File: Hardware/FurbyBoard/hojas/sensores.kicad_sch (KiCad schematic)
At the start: 37 parts, among them J7 Frente: IR (emisor ×2, recept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, J8 Inclinación ×3, lengua ×2, al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, J9 Encoder ×3, leva ×2, barriga 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, Q3 AO3400A, U10 TCA9535PWR, U11 SN74LVC1G17DBVR

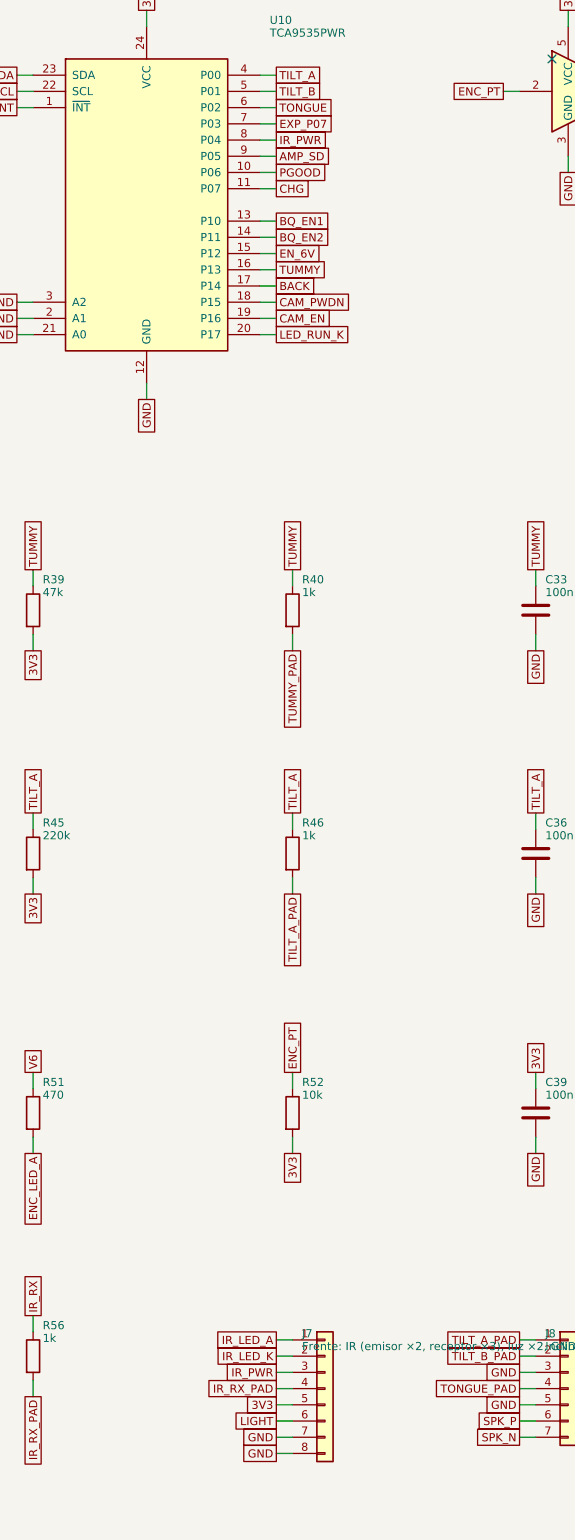
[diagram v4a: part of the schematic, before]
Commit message: Feature: IR_PWR rutado de U10 a J7 (bloque U2, 0 sin unir)
- Puertos del TCA9535 en ciclo: P03 LED_RUN_K, P04 EXP_P07, P17 IR_PWR;
  J7.3 <-> J7.8 (IR_PWR a J7.8 «RXV», J7.3 a GND). Rótulos de J7 y J_EXP.5.
- IR_PWR: vía que era de LED_RUN_K, columna de In3 x -91,4 entre LED_RUN_K
  y TUMMY, bolsa de In3 hasta una vía bajo J7.8 y In2 recto al pad.
- I2C_SCL: ramal de J11 desde la vía de U10.22 por In2 bajo U10; ramal de
  J6 a una vía nueva y B.Cu a la fila de y -69; R37.1 con 0,3.
- TONGUE recto a C35.1 y R43 0,13 mm al sur para la vía de EXP_P07.

Puerta D: ERC 0; DRC con paridad 0 violaciones, 0 sin unir, 0 paridad
(también con relleno sobre una copia); revisar-rutado PASS, 0 errores y
152 avisos (153 antes). PNG revisados: U10 (F, In3) y franja U10-J7
(F, In2, In3, B). Rellenos: GND In1/In4 1 trozo; VSYS In2 2584,5 mm² en 3
(se pierde la bolsa sin cargas bajo J7); GND F 21 y GND B 11 trozos, los
nuevos colgados del pad de J7.3.

Co-Authored-By: Claude Opus 5.5 (1M context) <noreply@anthropic.com>
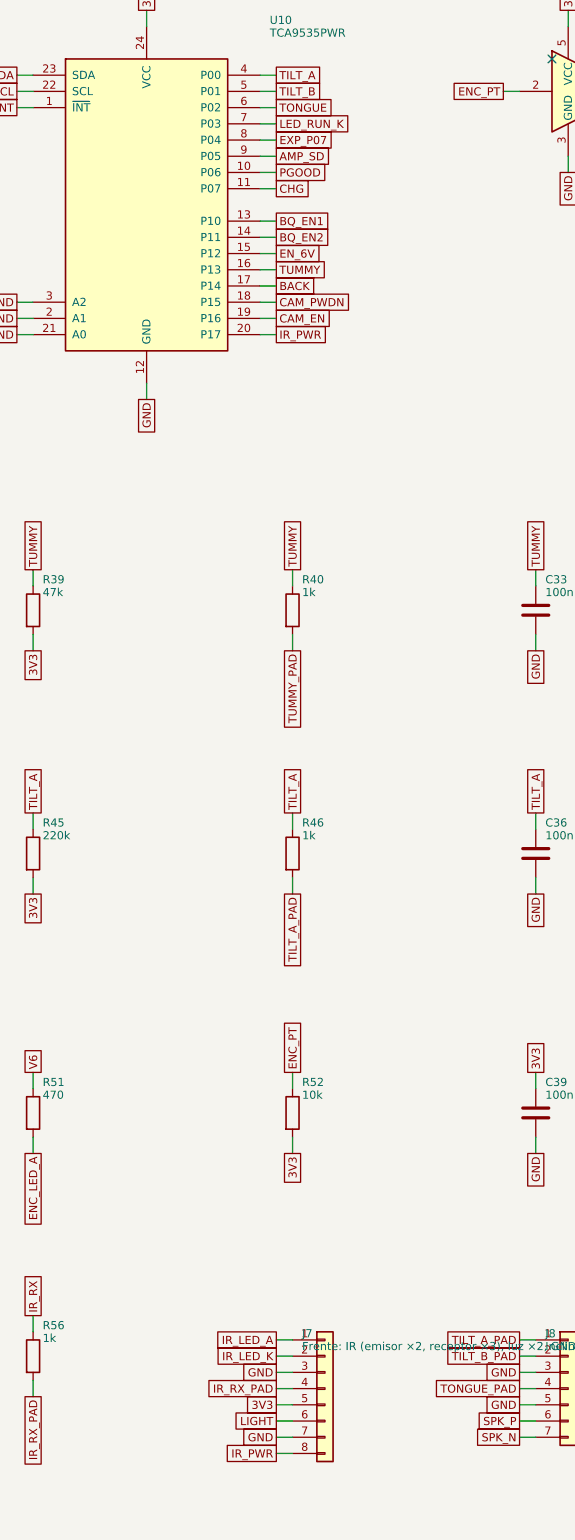
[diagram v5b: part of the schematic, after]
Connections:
- net EXP_P07: now also U10.8 (P04); no longer U10.7 (P03)
- net GND: now also J7.3 (Pin_3); no longer J7.8 (Pin_8)
- net IR_PWR: now also J7.8 (Pin_8), U10.20 (P17); no longer J7.3 (Pin_3), U10.8 (P04)
- net LED_RUN_K: now also U10.7 (P03); no longer U10.20 (P17)

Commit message: Docs: notas del esquema y descripción de D5 al día con el mapa de pines final
Las notas de las hojas seguían con pines de antes del replanteo: JP1 libera
GPIO9 (no GPIO48), la INT del TCA9535 va a GPIO6 (no GPIO21), JP4 libera GPIO8
(no GPIO14) y el LED del encoder va desde V6 por 470 Ω (sin AO3400A); LED RUN en
P03 (no P16) y J_EXP 2 × 5 con el orden del bloque U. Sin cambios de redes.

Puertas: ERC 0, DRC con paridad 0/0 y 0 sin unir; cobre y rellenos idénticos.

Co-Authored-By: Claude Opus 5.5 (1M context) <noreply@anthropic.com>
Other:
- note added: "Encoder: LED IR desde V6 por 470 Ω (luce con EN_6V) y fototransistor al Schmitt; JP4 libera GPIO8."
- note added: "TCA9535 en 0x20, mismo I2C que el SCCB de la cámara; INT a GPIO6 (despierta del sueño)."
- note removed: "Encoder: LED IR con AO3400A en EN_6V y fototransistor al Schmitt; JP4 libera GPIO14."
- note removed: "TCA9535 en 0x20, mismo I2C que el SCCB de la cámara; INT a GPIO21 (despierta del sueño)."
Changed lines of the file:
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@@
 		)
 	)
-	(text "Encoder: LED IR con AO3400A en EN_6V y fototransistor al Schmitt; JP4 libera GPIO14."
+	(text "Encoder: LED IR desde V6 por 470 Ω (luce con EN_6V) y fototransistor al Schmitt; JP4 libera GPIO8."
 		(exclude_from_sim no)
 		(at 20 38 0)
@@
 		)
 	)
-	(text "TCA9535 en 0x20, mismo I2C que el SCCB de la cámara; INT a GPIO21 (despierta del sueño)."
+	(text "TCA9535 en 0x20, mismo I2C que el SCCB de la cámara; INT a GPIO6 (despierta del sueño)."
 		(exclude_from_sim no)
 		(at 20 30 0)

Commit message: Fix: LED del encoder desde EN_6V y no desde V6 (revisión E independiente, I3)
El TPS61089 no desconecta la carga: con EN bajo, V6 = VSYS - 0,4 V por el
diodo del FET alto (SLVSD38C), así que el LED del encoder (R51 desde V6)
gastaba 2,8-5,3 mA también dormido, frente a los ~80 uA del requisito.

- R51 de 220 ohm (C22962, básica) desde EN_6V (P12 del TCA9535, push-pull):
  luce solo con el elevador encendido. TCA9535 (SCPS201F): VOH >= 2,6 V a
  -8 mA con VCC 3 V -> 5,4 mA en el peor caso bajo, ~8 mA típico, <= 10,4 mA
  de cota (IOH recomendada 10 mA). EN_6V >= 2,6 V >> VEN_H 1,2 V.
- Ruta: vía de EN_6V junto a U5 a (-48,4; -118,25) y B.Cu por x -48,4,
  y -108,4 y el pasillo x -45,8 del antiguo ramal de V6 hasta R51; la vía
  de V6 (-46,55; -106,3) queda unida por B.Cu a la de (-46,55; -107,41).
- NOTAS (Decisiones, Cálculos, Pines), README (J9.3, P12, diagrama) y
  TEST-PLAN (tensión en R51 con EN_6V = 1 y 0).

Puerta D: ERC 0; DRC con paridad 0, 0 sin unir (también con relleno de
kicad-cli sobre una copia); revisar-rutado 0 errores (151 avisos, 152
antes: una entrada asimétrica menos en R51); comprobar-flujo sin errores
nuevos. Rellenos de kicad-cli: In1/In4 3324,3 mm2 en 1, GND F 2096,9 en 21,
GND B 2790,9 en 10, VSYS In2 2584,4 en 3 (sin islas nuevas).
PNG revisados: B.Cu de U5 a R51 (pasillo x -45,8 entre C20/C22 y J9),
F.Cu de U5/C18/C16 (vía nueva de EN_6V) y F.Cu junto a R51.

Co-Authored-By: Claude Opus 5.5 (1M context) <noreply@anthropic.com>
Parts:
- R51: value 470 -> 220; LCSC C23179 -> C22962
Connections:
- net V6 is gone; now on net EN_6V: R51.1
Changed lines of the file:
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@@
 		)
 	)
-	(global_label "V6"
+	(global_label "EN_6V"
 		(shape passive)
 		(at 48.26 229.87 90)
@@
 			)
 		)
-		(property "Value" "470"
+		(property "Value" "220"
 			(at 49.76 233.41 0)
 			(show_name no)
@@
 			)
 		)
-		(property "Description" "LED del encoder ≈ 10 mA con el elevador encendido"
+		(property "Description" "LED del encoder ≈ 8 mA solo con EN_6V = 1"
 			(at 48.26 236.22 0)
 			(hide yes)
@@
 			)
 		)
-		(property "LCSC" "C23179"
+		(property "LCSC" "C22962"
 			(at 48.26 236.22 0)
 			(hide yes)
